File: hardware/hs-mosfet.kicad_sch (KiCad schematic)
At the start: 17 parts, among them Q301 2N7002

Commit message: Restore robust hardware project state and clean up test files
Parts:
- added C303, C304: 0.1u, symbol Device:C_Small
- added D1, D2, D3: BAT46, Diode_THT:D_DO-35_SOD27_P7.62mm_Horizontal, symbol Diode:BAT46
- added D203, D204: BZT52B82, Diode_SMD:D_SOD-123F, symbol Diode:BZT52Bxx
- added D306: 1N4148W, Diode_SMD:D_SOD-123, symbol Diode:1N4148W
- added D308: BZT52B5V1, symbol Diode:BZT52Bxx
- added Q302: IRLML6402, Package_TO_SOT_SMD:SOT-23, symbol Simulation_SPICE:PMOS
- added R134: 511, symbol Device:R
- added R205: 5.1k, Resistor_SMD:R_0402_1005Metric, symbol Device:R_Small
- added R231, R232: 49.9k, Resistor_SMD:R_0402_1005Metric, symbol Device:R_Small
- added R233, R234: 20k, Resistor_SMD:R_0402_1005Metric, symbol Device:R_Small
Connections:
- net BAT+: now also D305.1 (K), C303.2
- net DSG: now also D306.1 (K)
- net GND: now also D305.2 (A), C304.1, D203.2 (A), D204.2 (A), D306.2 (A)
- net MOSFET-CASCADE-DSG/GATE: now also D308.1 (K), Q302.3 (S); no longer R302.1, R303.1
- net PACK+: now also R134.1, R232.2, R233.2, R234.2
- net PGND: now also D2.2 (A), D3.2 (A)
- new net: D1.1 (K), D2.1 (K), R231.2, R233.1, R234.1
- new net: D3.1 (K), R205.2, R232.1
- new net: Q302.1 (D), R134.2
- new net: D308.2 (A), Q302.2 (G), R302.1, R303.1
- new net: C303.1, C304.2
- new net LD: D1.2 (A), D204.1 (K), R231.1
- new net PACK: D203.1 (K), R205.1
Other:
- added sheet PRE-CHG-MOSFET (Pre_Mosfet.kicad_sch)
- added sheet PRE-DSG-MOSFET (Pre_Mosfet.kicad_sch)
- note added: "Active Clamp Protection"
- note added: "Load dump"
- moved on the sheet: C301, C302, C305, C306, D301, D302, D303, D304, D305, Q301, R302, R303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

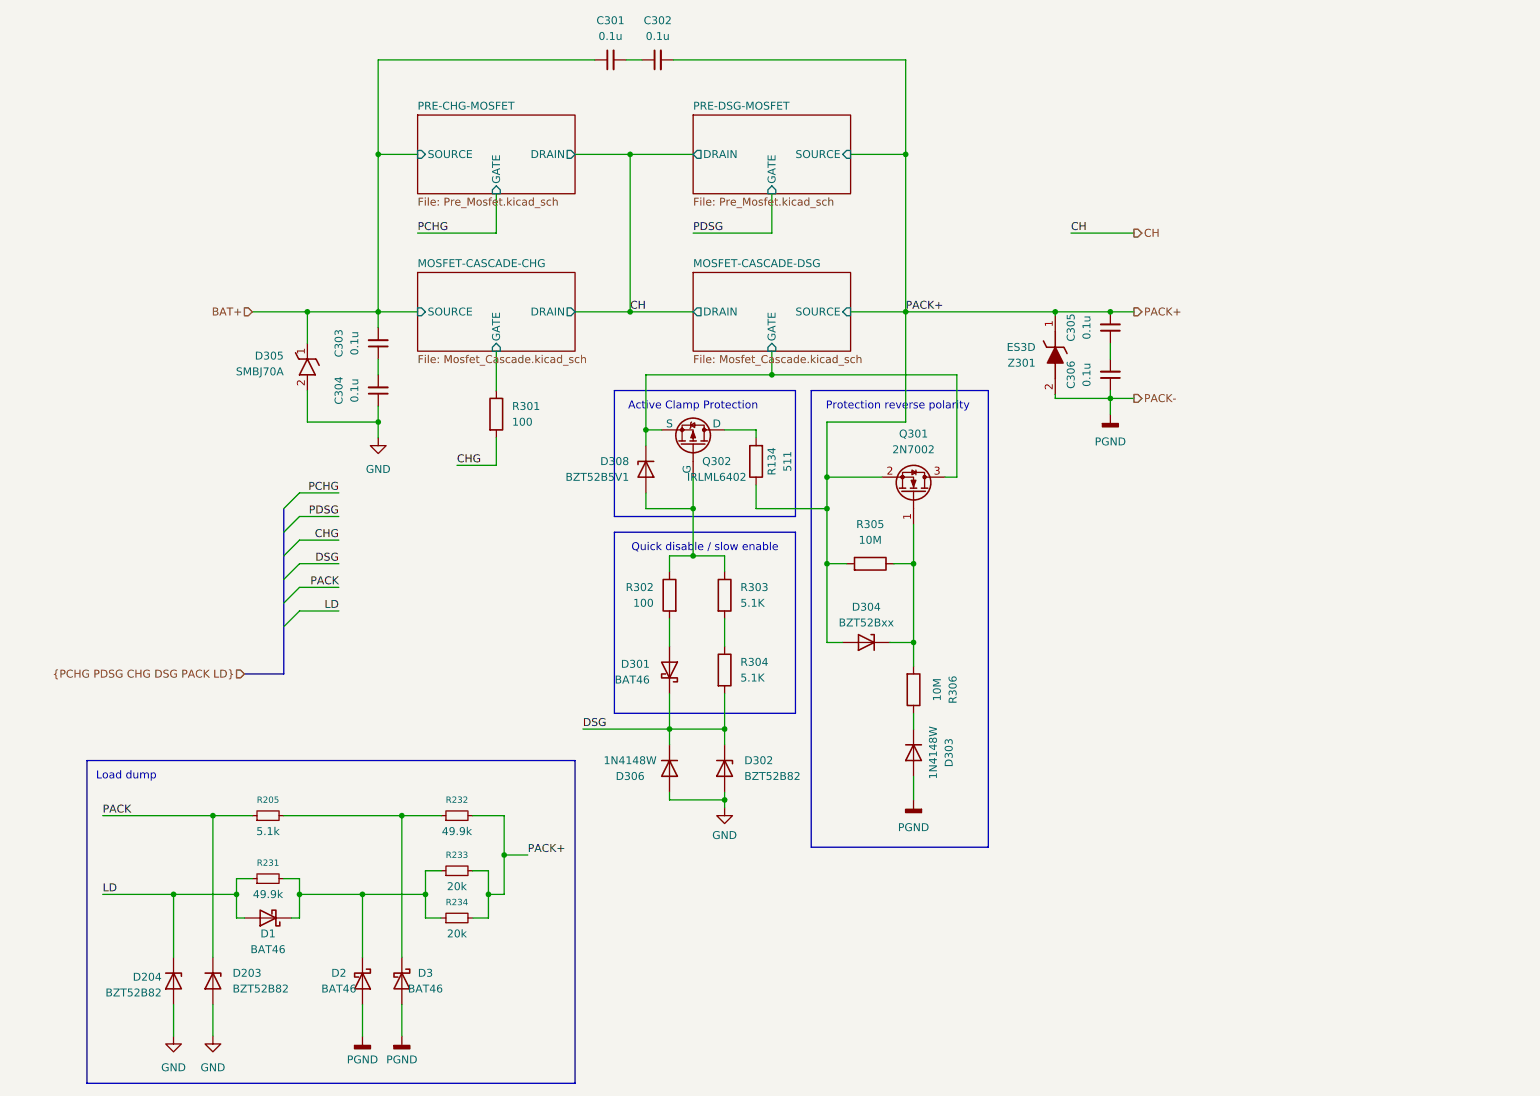
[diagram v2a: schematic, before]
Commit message: remove jetbrains mcps, add uv in home and update flake
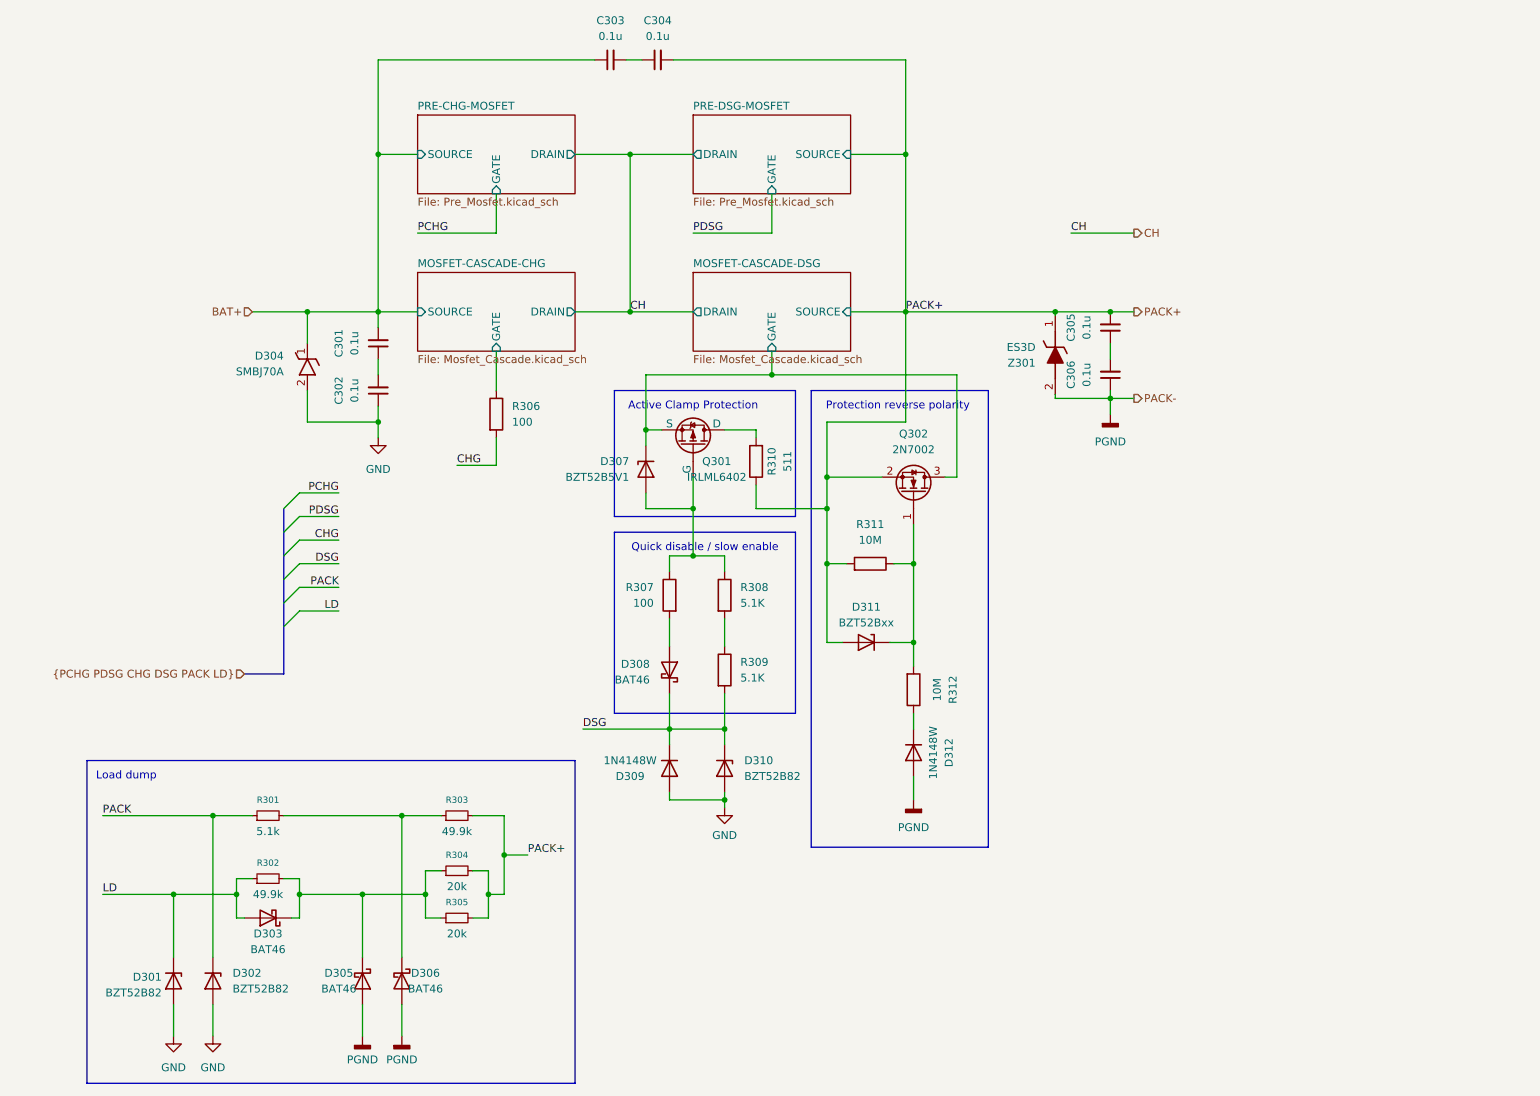
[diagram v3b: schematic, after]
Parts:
- renumbered C303 to C301, C304 to C302, C301 to C303, C302 to C304, D204 to D301, D203 to D302, D1 to D303, D305 to D304, D2 to D305, D3 to D306, D308 to D307, D301 to D308, D306 to D309, D302 to D310, D304 to D311, D303 to D312, Q302 to Q301, Q301 to Q302, R205 to R301, R231 to R302, R232 to R303, R233 to R304, R234 to R305, R301 to R306, R302 to R307, R303 to R308, R304 to R309, R134 to R310, R305 to R311, R306 to R312

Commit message: remove EN
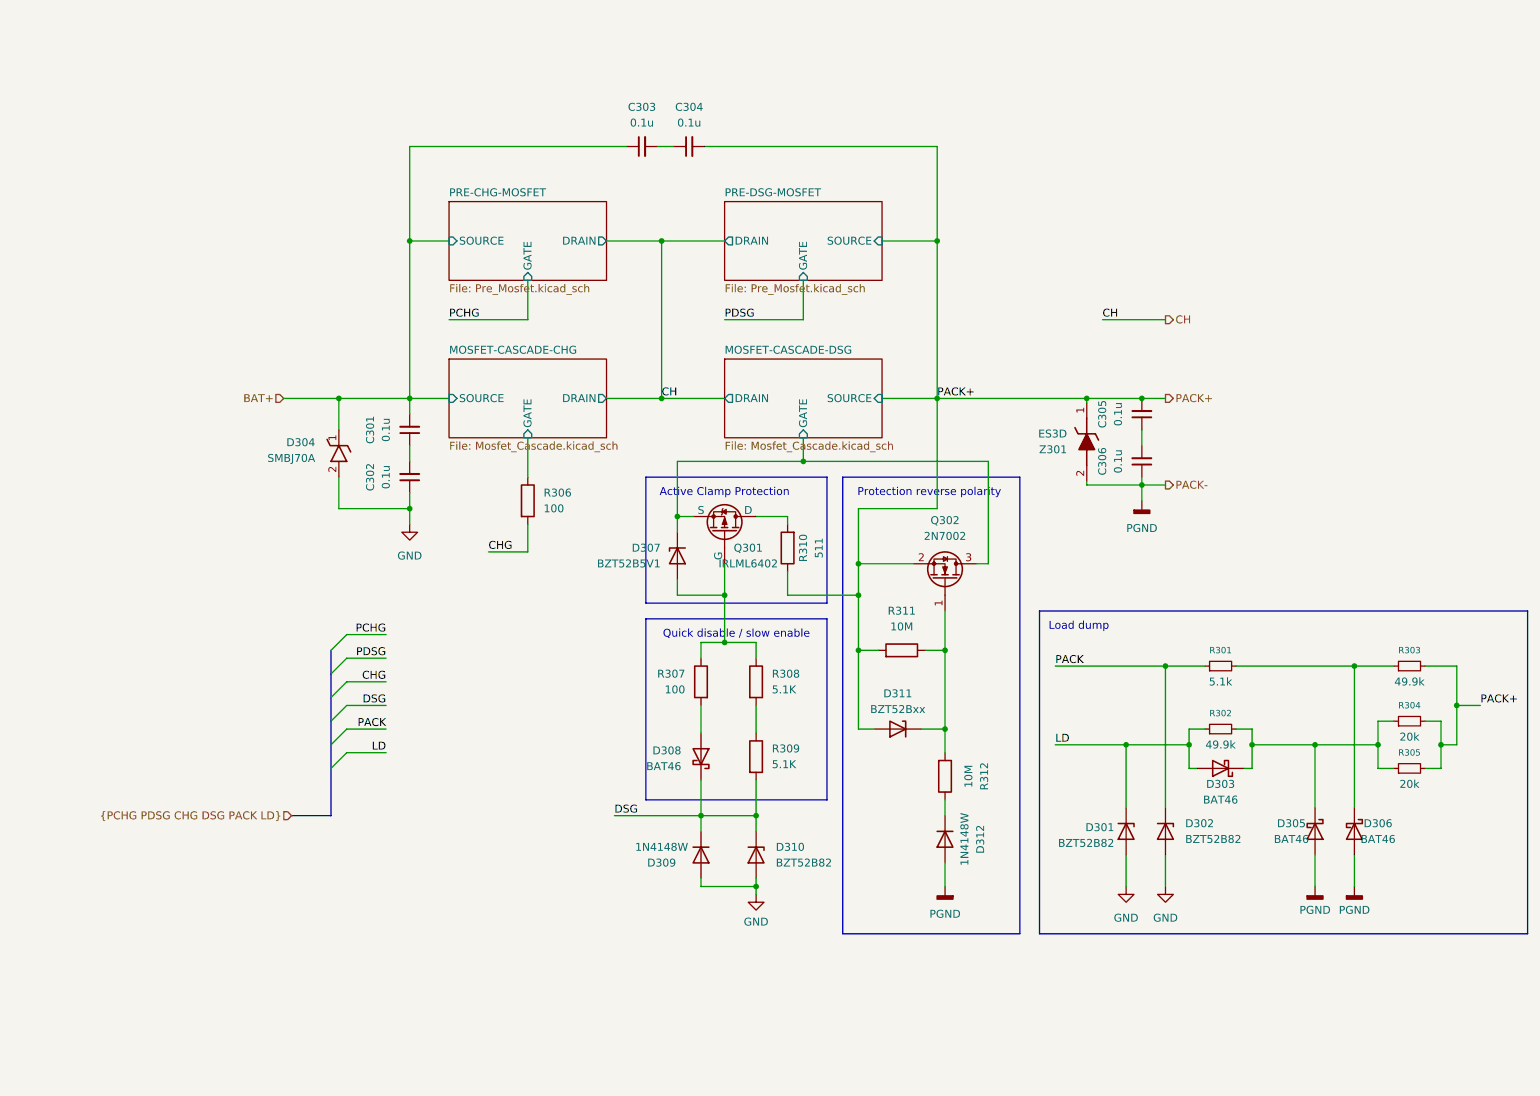
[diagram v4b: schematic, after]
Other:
- moved on the sheet: C301, C302, C303, C304, C305, C306, D301, D302, D303, D304, D305, D306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

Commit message: change props
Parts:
- renumbered D304 to D301, D307 to D302, D308 to D303, D309 to D304, D310 to D305, D311 to D306, D312 to D307, D301 to D308, D302 to D309, D303 to D310, D305 to D311, D306 to D312, R306 to R301, R307 to R302, R308 to R303, R309 to R304, R310 to R305, R311 to R306, R312 to R307, R301 to R308, R302 to R309, R303 to R310, R304 to R311, R305 to R312

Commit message: x
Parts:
- C301, C302, C303, C304, C305, C306: footprint (none) -> Capacitor_SMD:C_0805_2012Metric; LCSC (none) -> C14663
- R301, R302, R303, R304, R305, R306, R307: footprint (none) -> Resistor_SMD:R_0805_2012Metric
- R308, R309, R310, R311, R312: footprint Resistor_SMD:R_0402_1005Metric -> Resistor_SMD:R_0805_2012Metric
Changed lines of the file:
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@@
 			)
 		)
-		(property "Footprint" ""
+		(property "Footprint" "Resistor_SMD:R_0805_2012Metric"
 			(at 129.032 135.255 90)
 			(hide yes)
@@
 			)
 		)
-		(property "Footprint" "Resistor_SMD:R_0402_1005Metric"
+		(property "Footprint" "Resistor_SMD:R_0805_2012Metric"
 			(at 236.22 129.54 0)
 			(hide yes)
@@
 			)
 		)
-		(property "Footprint" ""
+		(property "Footprint" "Resistor_SMD:R_0805_2012Metric"
 			(at 159.512 138.43 90)
 			(hide yes)
@@
 			)
 		)
-		(property "Footprint" ""
+		(property "Footprint" "Resistor_SMD:R_0805_2012Metric"
 			(at 129.032 123.19 90)
 			(hide yes)
@@
 			)
 		)
-		(property "Footprint" ""
+		(property "Footprint" "Capacitor_SMD:C_0805_2012Metric"
 			(at 74.93 82.55 0)
 			(hide yes)
@@
 			)
 		)
+		(property "LCSC" "C14663"
+			(at 74.93 82.55 90)
+			(hide yes)
+			(show_name no)
+			(do_not_autoplace no)
+			(effects
+				(font
+					(size 1.27 1.27)
+				)
+			)
+		)
 		(pin "2"
 		)
@@
 			)
 		)
-		(property "Footprint" ""
+		(property "Footprint" "Resistor_SMD:R_0805_2012Metric"
 			(at 123.698 123.19 90)
 			(hide yes)
@@
 			)
 		)
-		(property "Footprint" "Resistor_SMD:R_0402_1005Metric"
+		(property "Footprint" "Resistor_SMD:R_0805_2012Metric"
 			(at 205.74 130.81 0)
 			(hide yes)
@@
 		(property "Footprint" ""
 			(at 118.11 102.87 0)
+			(hide yes)
 			(show_name no)
 			(do_not_autoplace no)
@@
 			)
 		)
-		(property "Footprint" ""
+		(property "Footprint" "Resistor_SMD:R_0805_2012Metric"
 			(at 154.305 119.888 90)
 			(hide yes)
@@
 			)
 		)
-		(property "Footprint" ""
+		(property "Footprint" "Resistor_SMD:R_0805_2012Metric"
 			(at 135.89 101.6 0)
+			(hide yes)
 			(show_name no)
 			(do_not_autoplace no)
@@
 			)
 		)
-		(property "Footprint" ""
+		(property "Footprint" "Capacitor_SMD:C_0805_2012Metric"
 			(at 74.93 90.17 0)
 			(hide yes)
@@
 			)
 		)
+		(property "LCSC" "C14663"
+			(at 74.93 90.17 90)
+			(hide yes)
+			(show_name no)
+			(do_not_autoplace no)
+			(effects
+				(font
+					(size 1.27 1.27)
+				)
+			)
+		)
 		(pin "2"
 		)
@@
 			)
 		)
-		(property "Footprint" "Resistor_SMD:R_0402_1005Metric"
+		(property "Footprint" "Resistor_SMD:R_0805_2012Metric"
 			(at 236.22 137.16 0)
 			(hide yes)
@@
 			)
 		)
-		(property "Footprint" ""
+		(property "Footprint" "Capacitor_SMD:C_0805_2012Metric"
 			(at 193.04 87.63 0)
 			(hide yes)
@@
 			)
 		)
+		(property "LCSC" "C14663"
+			(at 193.04 87.63 90)
+			(hide yes)
+			(show_name no)
+			(do_not_autoplace no)
+			(effects
+				(font
+					(size 1.27 1.27)
+				)
+			)
+		)
 		(pin "2"
 		)
@@
 			)
 		)
-		(property "Footprint" ""
+		(property "Footprint" "Resistor_SMD:R_0805_2012Metric"
 			(at 92.202 93.98 90)
 			(hide yes)
@@
 			)
 		)
-		(property "Footprint" ""
+		(property "Footprint" "Capacitor_SMD:C_0805_2012Metric"
 			(at 120.015 36.83 0)
 			(hide yes)
@@
 			)
 		)
+		(property "LCSC" "C14663"
+			(at 120.015 36.83 90)
+			(hide yes)
+			(show_name no)
+			(do_not_autoplace no)
+			(effects
+				(font
+					(size 1.27 1.27)
+				)
+			)
+		)
 		(pin "2"
 		)
@@
 			)
 		)
-		(property "Footprint" ""
+		(property "Footprint" "Capacitor_SMD:C_0805_2012Metric"
 			(at 193.04 80.01 0)
 			(hide yes)
@@
 			)
 		)
+		(property "LCSC" "C14663"
+			(at 193.04 80.01 90)
+			(hide yes)
+			(show_name no)
+			(do_not_autoplace no)
+			(effects
+				(font
+					(size 1.27 1.27)
+				)
+			)
+		)
 		(pin "2"
 		)
@@
 			)
 		)
-		(property "Footprint" "Resistor_SMD:R_0402_1005Metric"
+		(property "Footprint" "Resistor_SMD:R_0805_2012Metric"
 			(at 205.74 120.65 0)
 			(hide yes)
@@
 			)
 		)
-		(property "Footprint" ""
+		(property "Footprint" "Capacitor_SMD:C_0805_2012Metric"
 			(at 112.395 36.83 0)
 			(hide yes)
@@
 			)
 		)
+		(property "LCSC" "C14663"
+			(at 112.395 36.83 90)
+			(hide yes)
+			(show_name no)
+			(do_not_autoplace no)
+			(effects
+				(font
+					(size 1.27 1.27)
+				)
+			)
+		)
 		(pin "2"
 		)
@@
 			)
 		)
-		(property "Footprint" "Resistor_SMD:R_0402_1005Metric"
+		(property "Footprint" "Resistor_SMD:R_0805_2012Metric"
 			(at 236.22 120.65 0)
 			(hide yes)

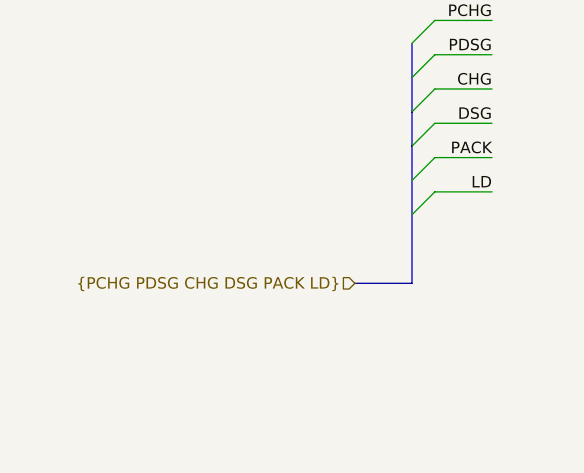
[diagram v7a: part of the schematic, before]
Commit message: use bus alias
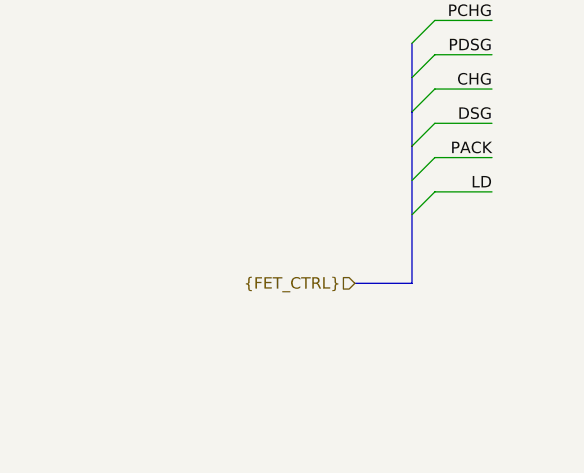
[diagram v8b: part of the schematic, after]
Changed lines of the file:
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@@
 		)
 	)
-	(hierarchical_label "{PCHG PDSG CHG DSG PACK LD}"
+	(hierarchical_label "{FET_CTRL}"
 		(shape input)
 		(at 55.88 144.78 180)
